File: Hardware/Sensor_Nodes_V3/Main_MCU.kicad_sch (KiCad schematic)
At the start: 22 parts, among them J2 Conn_01x27_Socket, J3 Conn_01x27_Socket, U2 STM32G474RBTx, U3 MCP2542FDxMF, U4 MCP2542FDxMF

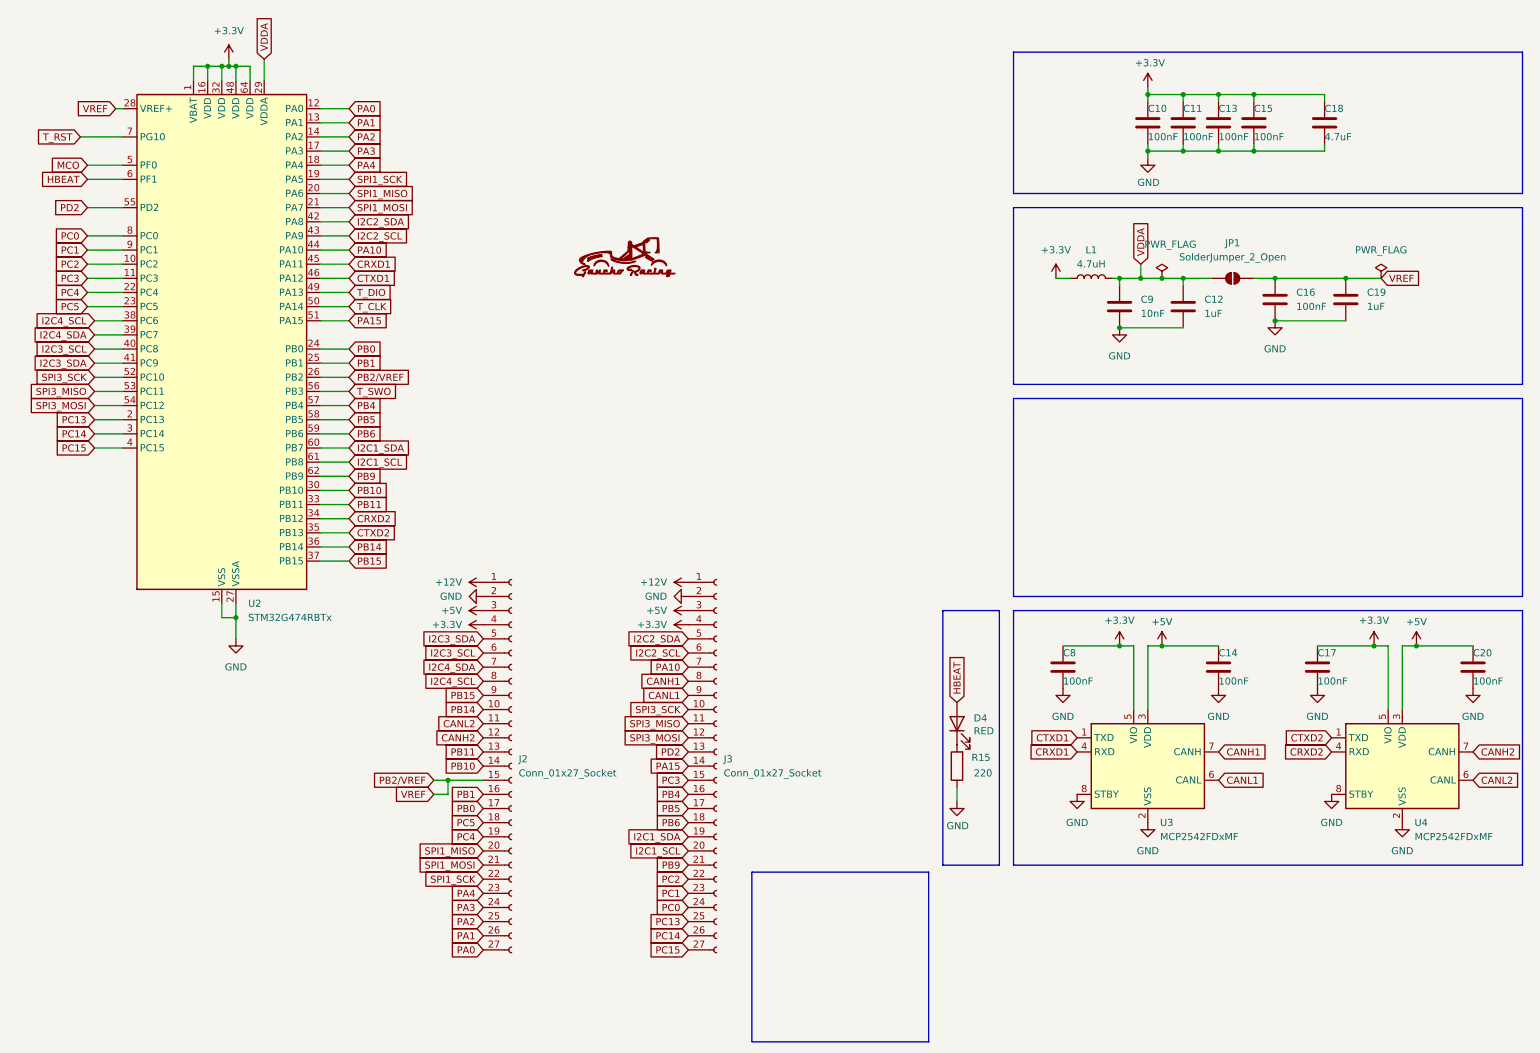
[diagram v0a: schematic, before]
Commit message: added a neopixel and moved some pins around
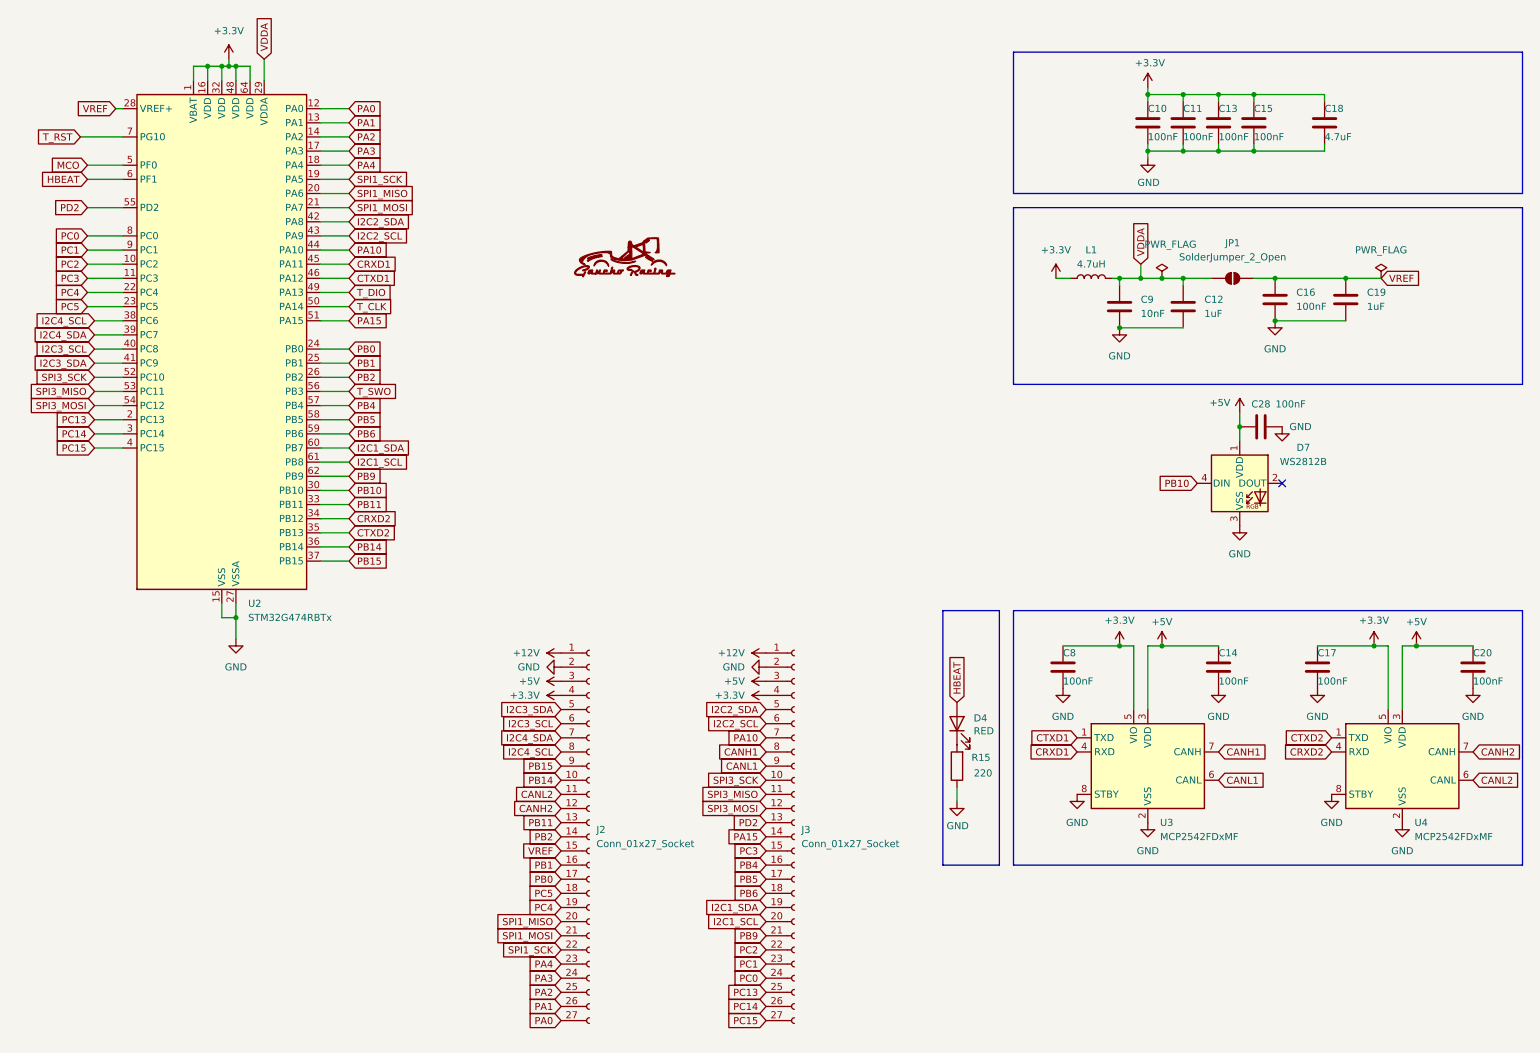
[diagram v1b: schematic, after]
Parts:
- added C28: 100nF, Capacitor_SMD:C_0603_1608Metric, symbol Device:C
- added D7: WS2812B, LED_SMD:LED_WS2812B_PLCC4_5.0x5.0mm_P3.2mm, symbol LED:WS2812B
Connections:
- net +5V: now also C28.2, D7.1 (VDD)
- net GND: now also C28.1, D7.3 (VSS)
- net PB10: now also D7.4 (DIN); no longer J2.14 (Pin_14)
- net PB2/VREF renamed VREF
- net VREF: no longer U2.26 (PB2)
- new net PB2: J2.14 (Pin_14), U2.26 (PB2)
- no-connect marks 0 -> 1
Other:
- moved on the sheet: J2, J3

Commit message: SAM V3.3 I think correct push
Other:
- moved on the sheet: C28, D7, U2
